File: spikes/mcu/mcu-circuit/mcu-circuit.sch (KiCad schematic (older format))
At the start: 8 parts

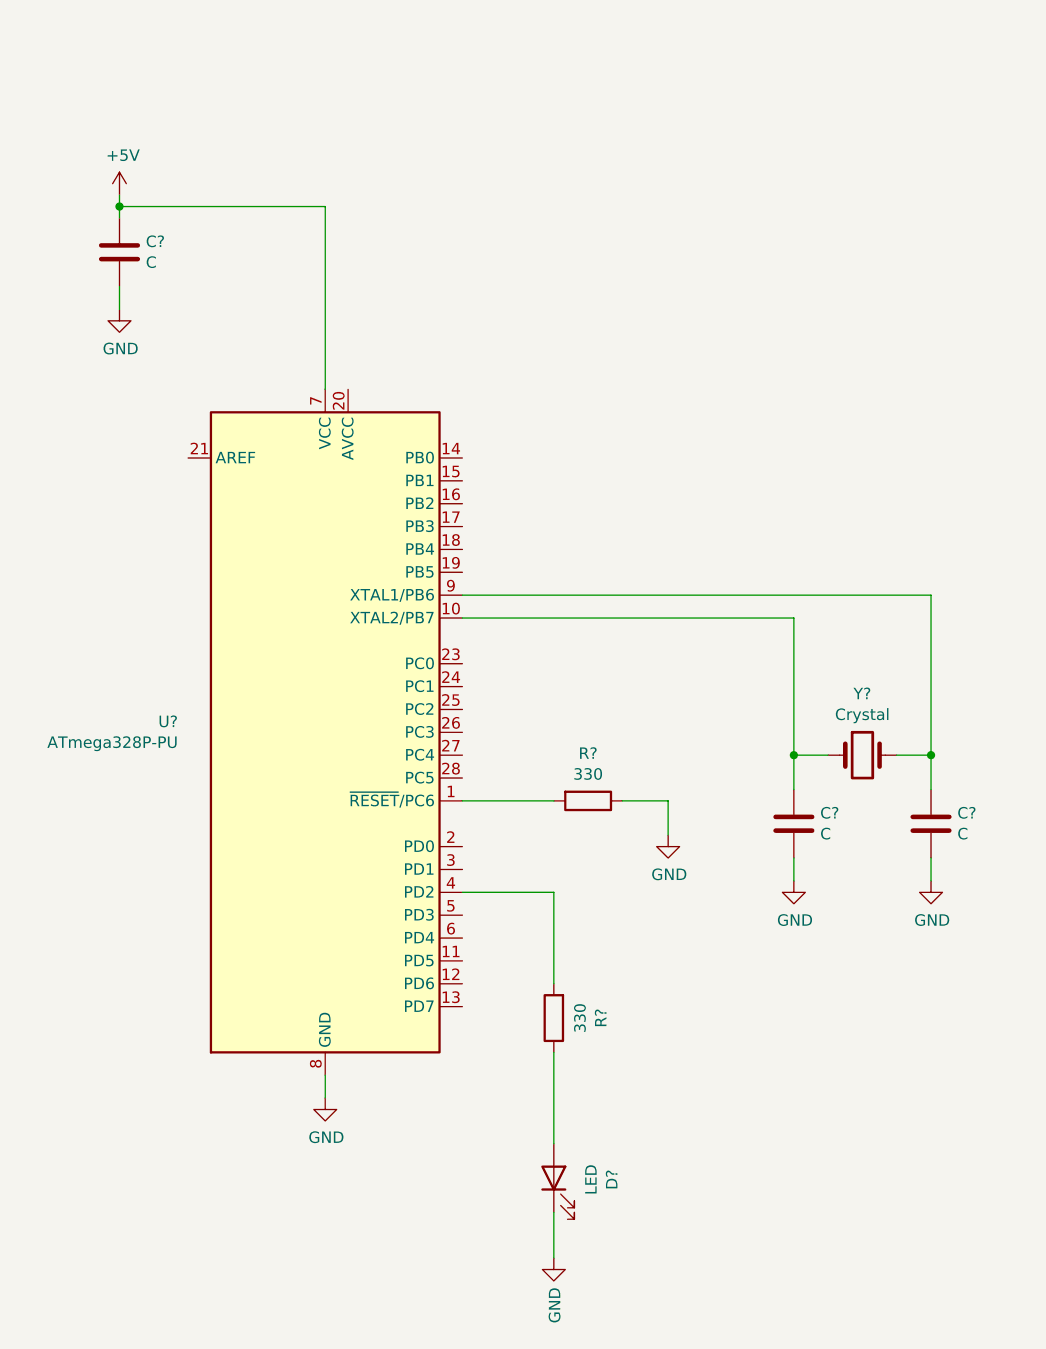
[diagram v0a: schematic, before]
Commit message: updated circuit for spike
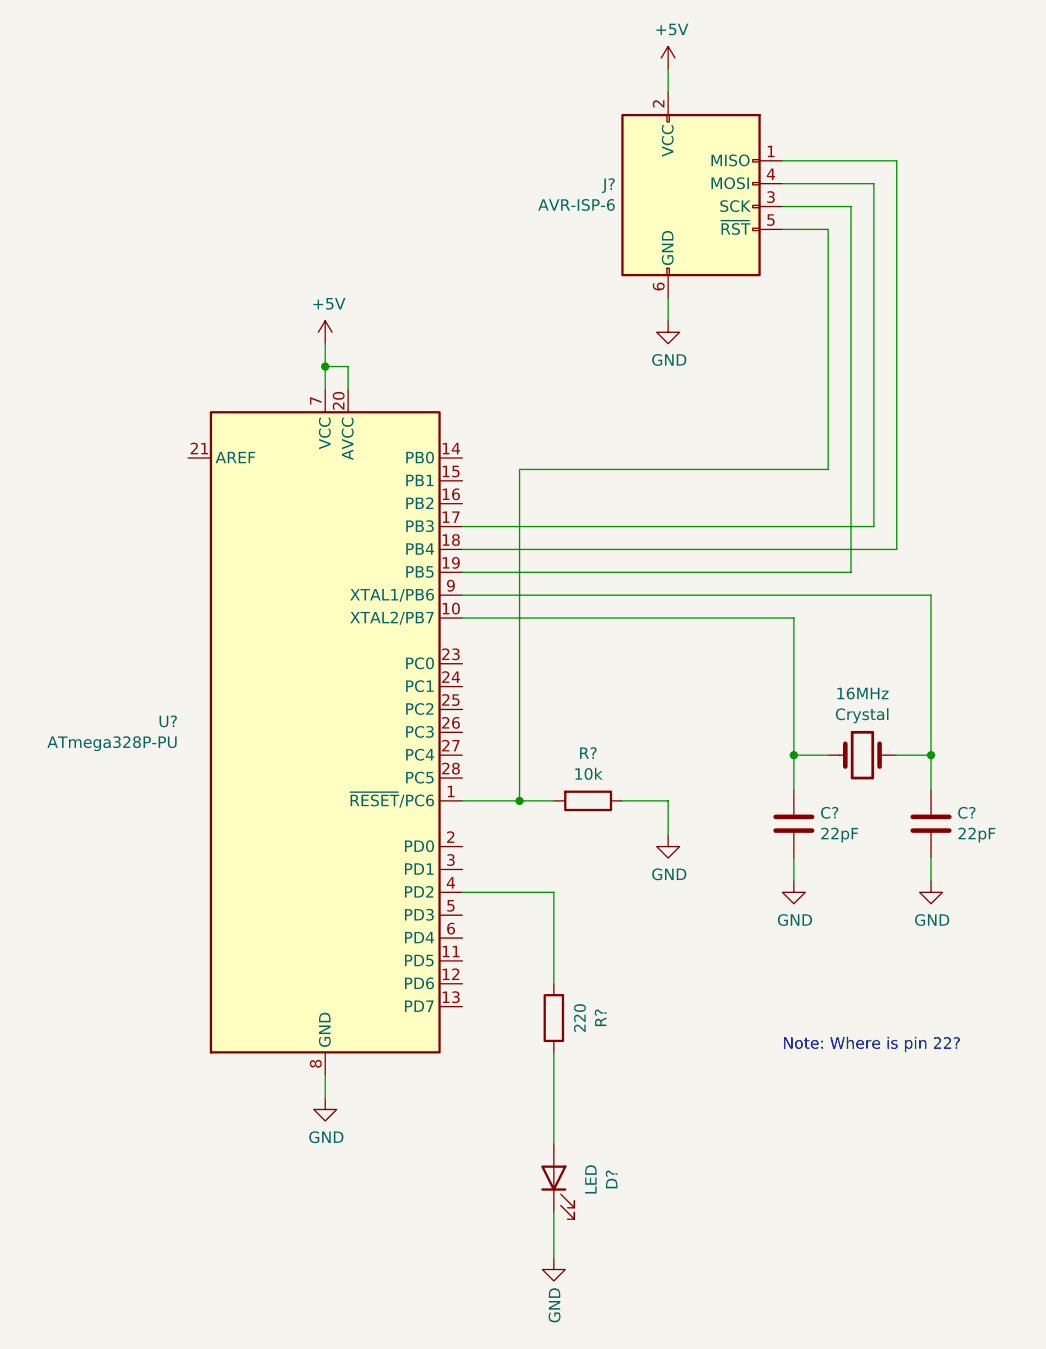
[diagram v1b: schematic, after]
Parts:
- removed C?: C, symbol Device:C
- added J?: AVR-ISP-6, symbol Connector:AVR-ISP-6
- C? (x2): value C -> 22pF
- R?: value 330 -> 10k
- R?: value 330 -> 220
- gave numbers to parts that had none: 1
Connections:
- net +5V: now also U?.20 (AVCC), J?.2 (VCC)
- net GND: now also J?.6 (GND)
- net at R?.2, U?.1 (~RESET~/PC6): now also J?.5 (~RST)
- net at U?.17 (PB3): now also J?.4 (MOSI)
- net at U?.18 (PB4): now also J?.1 (MISO)
- net at U?.19 (PB5): now also J?.3 (SCK)
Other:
- note added: "Note: Where is pin 22?"
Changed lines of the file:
@@
 P 3900 3950
 F 0 "R?" V 3693 3950 50  0000 C CNN
-F 1 "330" V 3784 3950 50  0000 C CNN
+F 1 "10k" V 3784 3950 50  0000 C CNN
 F 2 "" V 3830 3950 50  0001 C CNN
 F 3 "~" H 3900 3950 50  0001 C CNN
@@
 $EndComp
 Wire Wire Line
-	3350 3950 3750 3950
+	3350 3950 3600 3950
 $Comp
 L Device:R R?
@@
 P 3750 4900
 F 0 "R?" V 3543 4900 50  0000 C CNN
-F 1 "330" V 3634 4900 50  0000 C CNN
+F 1 "220" V 3634 4900 50  0000 C CNN
 F 2 "" V 3680 4900 50  0001 C CNN
 F 3 "~" H 3750 4900 50  0001 C CNN
@@
 	3750 5750 3750 5950
 $Comp
-L Device:C C?
-U 1 1 61312620
-P 1850 1550
-F 0 "C?" H 1965 1596 50  0000 L CNN
-F 1 "C" H 1965 1505 50  0000 L CNN
-F 2 "" H 1888 1400 50  0001 C CNN
-F 3 "~" H 1850 1550 50  0001 C CNN
-	1    1850 1550
-	1    0    0    -1
-$EndComp
-$Comp
 L power:+5V #PWR?
 U 1 1 613144DB
-P 1850 1300
-F 0 "#PWR?" H 1850 1150 50  0001 C CNN
-F 1 "+5V" H 1865 1473 50  0000 C CNN
-F 2 "" H 1850 1300 50  0001 C CNN
-F 3 "" H 1850 1300 50  0001 C CNN
-	1    1850 1300
-	1    0    0    -1
-$EndComp
-$Comp
-L power:GND #PWR?
-U 1 1 613149A1
-P 1850 1800
-F 0 "#PWR?" H 1850 1550 50  0001 C CNN
-F 1 "GND" H 1855 1627 50  0000 C CNN
-F 2 "" H 1850 1800 50  0001 C CNN
-F 3 "" H 1850 1800 50  0001 C CNN
-	1    1850 1800
-	1    0    0    -1
-$EndComp
-Wire Wire Line
-	1850 1400 1850 1350
-Wire Wire Line
-	1850 1700 1850 1800
-Wire Wire Line
-	2750 1350 1850 1350
-Wire Wire Line
-	2750 1350 2750 2150
-Connection ~ 1850 1350
-Wire Wire Line
-	1850 1350 1850 1300
+P 2750 1950
+F 0 "#PWR?" H 2750 1800 50  0001 C CNN
+F 1 "+5V" H 2765 2123 50  0000 C CNN
+F 2 "" H 2750 1950 50  0001 C CNN
+F 3 "" H 2750 1950 50  0001 C CNN
+	1    2750 1950
+	1    0    0    -1
+$EndComp
 $Comp
 L power:GND #PWR?
@@
 	2750 5250 2750 5150
 $Comp
-L Device:Crystal Y?
+L Device:Crystal 16MHz
 U 1 1 613236AE
 P 5100 3750
-F 0 "Y?" H 5100 4018 50  0000 C CNN
+F 0 "16MHz" H 5100 4018 50  0000 C CNN
 F 1 "Crystal" H 5100 3927 50  0000 C CNN
 F 2 "" H 5100 3750 50  0001 C CNN
@@
 P 4800 4050
 F 0 "C?" H 4915 4096 50  0000 L CNN
-F 1 "C" H 4915 4005 50  0000 L CNN
+F 1 "22pF" H 4915 4005 50  0000 L CNN
 F 2 "" H 4838 3900 50  0001 C CNN
 F 3 "~" H 4800 4050 50  0001 C CNN
@@
 P 5400 4050
 F 0 "C?" H 5515 4096 50  0000 L CNN
-F 1 "C" H 5515 4005 50  0000 L CNN
+F 1 "22pF" H 5515 4005 50  0000 L CNN
 F 2 "" H 5438 3900 50  0001 C CNN
 F 3 "~" H 5400 4050 50  0001 C CNN
@@
 Wire Wire Line
 	3350 4350 3750 4350
+Wire Wire Line
+	2750 1950 2750 2050
+Wire Wire Line
+	2750 2050 2850 2050
+Wire Wire Line
+	2850 2050 2850 2150
+Connection ~ 2750 2050
+Wire Wire Line
+	2750 2050 2750 2150
+Text Notes 4750 5050 0    50   ~ 0
+Note: Where is pin 22?
+$Comp
+L Connector:AVR-ISP-6 J?
+U 1 1 6133DCED
+P 4350 1350
+F 0 "J?" H 4021 1446 50  0000 R CNN
+F 1 "AVR-ISP-6" H 4021 1355 50  0000 R CNN
+F 2 "" V 4100 1400 50  0001 C CNN
+F 3 " ~" H 3075 800 50  0001 C CNN
+	1    4350 1350
+	1    0    0    -1
+$EndComp
+$Comp
+L power:GND #PWR?
+U 1 1 6133F32F
+P 4250 1850
+F 0 "#PWR?" H 4250 1600 50  0001 C CNN
+F 1 "GND" H 4255 1677 50  0000 C CNN
+F 2 "" H 4250 1850 50  0001 C CNN
+F 3 "" H 4250 1850 50  0001 C CNN
+	1    4250 1850
+	1    0    0    -1
+$EndComp
+$Comp
+L power:+5V #PWR?
+U 1 1 6133F8B2
+P 4250 750
+F 0 "#PWR?" H 4250 600 50  0001 C CNN
+F 1 "+5V" H 4265 923 50  0000 C CNN
+F 2 "" H 4250 750 50  0001 C CNN
+F 3 "" H 4250 750 50  0001 C CNN
+	1    4250 750
+	1    0    0    -1
+$EndComp
+Wire Wire Line
+	4250 750  4250 850
+Wire Wire Line
+	4250 1750 4250 1850
+Wire Wire Line
+	4750 1250 5150 1250
+Wire Wire Line
+	5150 1250 5150 2750
+Wire Wire Line
+	5150 2750 3350 2750
+Wire Wire Line
+	4750 1150 5250 1150
+Wire Wire Line
+	5250 1150 5250 2850
+Wire Wire Line
+	5250 2850 3350 2850
+Wire Wire Line
+	3350 2950 5050 2950
+Wire Wire Line
+	3600 2500 3600 3950
+Connection ~ 3600 3950
+Wire Wire Line
+	3600 3950 3750 3950
+Wire Wire Line
+	5050 1350 5050 2950
+Wire Wire Line
+	5050 1350 4750 1350
+Wire Wire Line
+	4950 1450 4950 2500
+Wire Wire Line
+	4750 1450 4950 1450
+Wire Wire Line
+	3600 2500 4950 2500
 $EndSCHEMATC

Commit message: lcd and mcu
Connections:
- net +5V: now also R?.1
- net GND: no longer R?.1
- net RESET: now reaches J?.5 (~RST), R?.2, U?.1 (~RESET~/PC6)
- net MOSI: now reaches J?.4 (MOSI), U?.17 (PB3)
- net MISO: now reaches J?.1 (MISO), U?.18 (PB4)
- net SCK: now reaches J?.3 (SCK), U?.19 (PB5)
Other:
- note removed: "Note: Where is pin 22?"
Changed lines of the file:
@@
 	0    1    1    0
 $EndComp
-Wire Wire Line
-	3350 3950 3600 3950
 $Comp
 L Device:R R?
@@
 	5400 3050 5400 3750
 Connection ~ 5400 3750
-$Comp
-L power:GND #PWR?
-U 1 1 6130CEF7
-P 4250 4100
-F 0 "#PWR?" H 4250 3850 50  0001 C CNN
-F 1 "GND" H 4255 3927 50  0000 C CNN
-F 2 "" H 4250 4100 50  0001 C CNN
-F 3 "" H 4250 4100 50  0001 C CNN
-	1    4250 4100
-	1    0    0    -1
-$EndComp
-Wire Wire Line
-	4250 3950 4250 4100
-Wire Wire Line
-	4050 3950 4250 3950
 Wire Wire Line
 	3350 4350 3750 4350
@@
 Wire Wire Line
 	2750 2050 2750 2150
-Text Notes 4750 5050 0    50   ~ 0
-Note: Where is pin 22?
 $Comp
 L Connector:AVR-ISP-6 J?
@@
 Wire Wire Line
 	4250 1750 4250 1850
-Wire Wire Line
-	4750 1250 5150 1250
-Wire Wire Line
-	5150 1250 5150 2750
-Wire Wire Line
-	5150 2750 3350 2750
-Wire Wire Line
-	4750 1150 5250 1150
-Wire Wire Line
-	5250 1150 5250 2850
-Wire Wire Line
-	5250 2850 3350 2850
-Wire Wire Line
-	3350 2950 5050 2950
-Wire Wire Line
-	3600 2500 3600 3950
-Connection ~ 3600 3950
-Wire Wire Line
-	3600 3950 3750 3950
-Wire Wire Line
-	5050 1350 5050 2950
-Wire Wire Line
-	5050 1350 4750 1350
-Wire Wire Line
-	4950 1450 4950 2500
-Wire Wire Line
-	4750 1450 4950 1450
-Wire Wire Line
-	3600 2500 4950 2500
+$Comp
+L power:+5V #PWR?
+U 1 1 613C4E61
+P 4150 3850
+F 0 "#PWR?" H 4150 3700 50  0001 C CNN
+F 1 "+5V" H 4165 4023 50  0000 C CNN
+F 2 "" H 4150 3850 50  0001 C CNN
+F 3 "" H 4150 3850 50  0001 C CNN
+	1    4150 3850
+	1    0    0    -1
+$EndComp
+Wire Wire Line
+	4050 3950 4150 3950
+Wire Wire Line
+	4150 3950 4150 3850
+Wire Wire Line
+	3350 3950 3450 3950
+Text Label 4750 1150 0    50   ~ 0
+MISO
+Text Label 4750 1250 0    50   ~ 0
+MOSI
+Text Label 4750 1350 0    50   ~ 0
+SCK
+Text Label 4750 1450 0    50   ~ 0
+RESET
+Text Label 3550 4100 0    50   ~ 0
+RESET
+Wire Wire Line
+	3550 4100 3450 4100
+Wire Wire Line
+	3450 4100 3450 3950
+Connection ~ 3450 3950
+Wire Wire Line
+	3450 3950 3750 3950
+Text Label 3350 2850 0    50   ~ 0
+MISO
+Text Label 3350 2750 0    50   ~ 0
+MOSI
+Text Label 3350 2950 0    50   ~ 0
+SCK
 $EndSCHEMATC
